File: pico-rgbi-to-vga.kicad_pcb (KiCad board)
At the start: 2 copper layers, 68.8 x 57 mm, 25 parts, among them J1 SDS-80J, J2 DB15_Female_HighDensity, J3 USB-B1HSB6, SW1 SW_Push, U1 Pico

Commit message: Fix label
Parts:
- RN1: value 20kΩ -> 15kΩ
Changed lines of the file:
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@@
     (descr "7-pin Resistor SIP pack")
     (tags "R")
+    (property "Mouser" "652-4607X-1LF-22K")
     (property "Sheetfile" "pico-rgbi-to-vga.kicad_sch")
     (property "Sheetname" "")
@@
       (effects (font (size 1 1) (thickness 0.15)))
     )
-    (fp_text value "20kΩ" (at 19.2 0.7 90) (layer "F.SilkS")
+    (fp_text value "15kΩ" (at 19.2 0.7 90) (layer "F.SilkS")
       (effects (font (size 1 1) (thickness 0.15)))
     )

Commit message: Use 8SIP for Vdiv pulldown, 7SIP is not available
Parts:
- RN1: footprint Resistor_THT:R_Array_SIP7 -> Resistor_THT:R_Array_SIP8
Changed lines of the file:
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@@
   (net 54 "+3V3")
   (net 55 "/SW_PALETTE_CHANGE")
+  (net 56 "unconnected-(RN1-Pad8)")
   (footprint "Resistor_SMD:R_0805_2012Metric_Pad1.20x1.40mm_HandSolder" (layer "F.Cu")
     (at 163.068 111.76)
@@
           ) (width 0) (fill yes))
       ))
+  )
+  (footprint "Resistor_THT:R_Array_SIP8" (layer "F.Cu")
+    (at 120.904 74.676 -90)
+    (descr "8-pin Resistor SIP pack")
+    (tags "R")
+    (property "Sheetfile" "pico-rgbi-to-vga.kicad_sch")
+    (property "Sheetname" "")
+    (attr through_hole)
+    (fp_text reference "RN1" (at -0.508 -2.4 90) (layer "F.SilkS")
+      (effects (font (size 1 1) (thickness 0.15)))
+    )
+    (fp_text value "15kΩ" (at 20.447 0.508 180) (layer "F.SilkS")
+      (effects (font (size 1 1) (thickness 0.15)))
+    )
+    (fp_text user "${REFERENCE}" (at 8.89 0 90) (layer "F.Fab")
+      (effects (font (size 1 1) (thickness 0.15)))
+    )
+    (fp_line (start -1.44 -1.4) (end -1.44 1.4) (layer "F.SilkS") (width 0.12))
+    (fp_line (start 19.22 -1.4) (end -1.44 -1.4) (layer "F.SilkS") (width 0.12))
+    (fp_line (start 1.27 -1.4) (end 1.27 1.4) (layer "F.SilkS") (width 0.12))
+    (fp_line (start -1.44 1.4) (end 19.22 1.4) (layer "F.SilkS") (width 0.12))
+    (fp_line (start 19.22 1.4) (end 19.22 -1.4) (layer "F.SilkS") (width 0.12))
+    (fp_line (start 19.5 1.65) (end 19.5 -1.65) (layer "F.CrtYd") (width 0.05))
+    (fp_line (start -1.7 1.65) (end 19.5 1.65) (layer "F.CrtYd") (width 0.05))
+    (fp_line (start 19.5 -1.65) (end -1.7 -1.65) (layer "F.CrtYd") (width 0.05))
+    (fp_line (start -1.7 -1.65) (end -1.7 1.65) (layer "F.CrtYd") (width 0.05))
+    (fp_line (start 19.07 -1.25) (end -1.29 -1.25) (layer "F.Fab") (width 0.1))
+    (fp_line (start 19.07 1.25) (end 19.07 -1.25) (layer "F.Fab") (width 0.1))
+    (fp_line (start 1.27 -1.25) (end 1.27 1.25) (layer "F.Fab") (width 0.1))
+    (fp_line (start -1.29 -1.25) (end -1.29 1.25) (layer "F.Fab") (width 0.1))
+    (fp_line (start -1.29 1.25) (end 19.07 1.25) (layer "F.Fab") (width 0.1))
+    (pad "1" thru_hole rect (at 0 0 270) (size 1.6 1.6) (drill 0.8) (layers *.Cu *.Mask)
+      (net 2 "GND") (pinfunction "common") (pintype "passive"))
+    (pad "2" thru_hole oval (at 2.54 0 270) (size 1.6 1.6) (drill 0.8) (layers *.Cu *.Mask)
+      (net 3 "/INTENS_IN") (pinfunction "R1") (pintype "passive"))
+    (pad "3" thru_hole oval (at 5.08 0 270) (size 1.6 1.6) (drill 0.8) (layers *.Cu *.Mask)
+      (net 5 "/VSYNC_IN") (pinfunction "R2") (pintype "passive"))
+    (pad "4" thru_hole oval (at 7.62 0 270) (size 1.6 1.6) (drill 0.8) (layers *.Cu *.Mask)
+      (net 4 "/HSYNC_IN") (pinfunction "R3") (pintype "passive"))
+    (pad "5" thru_hole oval (at 10.16 0 270) (size 1.6 1.6) (drill 0.8) (layers *.Cu *.Mask)
+      (net 8 "/BLUE_IN") (pinfunction "R4") (pintype "passive"))
+    (pad "6" thru_hole oval (at 12.7 0 270) (size 1.6 1.6) (drill 0.8) (layers *.Cu *.Mask)
+      (net 7 "/GREEN_IN") (pinfunction "R5") (pintype "passive"))
+    (pad "7" thru_hole oval (at 15.24 0 270) (size 1.6 1.6) (drill 0.8) (layers *.Cu *.Mask)
+      (net 6 "/RED_IN") (pinfunction "R6") (pintype "passive"))
+    (pad "8" thru_hole oval (at 17.78 0 270) (size 1.6 1.6) (drill 0.8) (layers *.Cu *.Mask)
+      (net 56 "unconnected-(RN1-Pad8)") (pinfunction "R7") (pintype "passive+no_connect"))
+    (model "${KICAD6_3DMODEL_DIR}/Resistor_THT.3dshapes/R_Array_SIP8.wrl"
+      (offset (xyz 0 0 0))
+      (scale (xyz 1 1 1))
+      (rotate (xyz 0 0 0))
+    )
   )
   (footprint "Resistor_SMD:R_0805_2012Metric_Pad1.20x1.40mm_HandSolder" (layer "F.Cu")
@@
       (offset (xyz 0 0 0))
       (scale (xyz 1 1 1))
-      (rotate (xyz 0 0 0))
-    )
-  )
-  (footprint "Resistor_THT:R_Array_SIP7" (layer "F.Cu")
-    (at 120.904 74.676 -90)
-    (descr "7-pin Resistor SIP pack")
-    (tags "R")
-    (property "Mouser" "652-4607X-1LF-22K")
-    (property "Sheetfile" "pico-rgbi-to-vga.kicad_sch")
-    (property "Sheetname" "")
-    (attr through_hole)
-    (fp_text reference "RN1" (at 18.7 -0.6 90) (layer "F.SilkS")
-      (effects (font (size 1 1) (thickness 0.15)))
-    )
-    (fp_text value "15kΩ" (at 19.2 0.7 90) (layer "F.SilkS")
-      (effects (font (size 1 1) (thickness 0.15)))
-    )
-    (fp_text user "${REFERENCE}" (at 7.62 0 90) (layer "F.Fab")
-      (effects (font (size 1 1) (thickness 0.15)))
-    )
-    (fp_line (start 16.68 1.4) (end 16.68 -1.4) (layer "F.SilkS") (width 0.12))
-    (fp_line (start -1.44 1.4) (end 16.68 1.4) (layer "F.SilkS") (width 0.12))
-    (fp_line (start 16.68 -1.4) (end -1.44 -1.4) (layer "F.SilkS") (width 0.12))
-    (fp_line (start 1.27 -1.4) (end 1.27 1.4) (layer "F.SilkS") (width 0.12))
-    (fp_line (start -1.44 -1.4) (end -1.44 1.4) (layer "F.SilkS") (width 0.12))
-    (fp_line (start -1.7 1.65) (end 16.95 1.65) (layer "F.CrtYd") (width 0.05))
-    (fp_line (start -1.7 -1.65) (end -1.7 1.65) (layer "F.CrtYd") (width 0.05))
-    (fp_line (start 16.95 -1.65) (end -1.7 -1.65) (layer "F.CrtYd") (width 0.05))
-    (fp_line (start 16.95 1.65) (end 16.95 -1.65) (layer "F.CrtYd") (width 0.05))
-    (fp_line (start 16.53 1.25) (end 16.53 -1.25) (layer "F.Fab") (width 0.1))
-    (fp_line (start -1.29 -1.25) (end -1.29 1.25) (layer "F.Fab") (width 0.1))
-    (fp_line (start -1.29 1.25) (end 16.53 1.25) (layer "F.Fab") (width 0.1))
-    (fp_line (start 16.53 -1.25) (end -1.29 -1.25) (layer "F.Fab") (width 0.1))
-    (fp_line (start 1.27 -1.25) (end 1.27 1.25) (layer "F.Fab") (width 0.1))
-    (pad "1" thru_hole rect (at 0 0 270) (size 1.6 1.6) (drill 0.8) (layers *.Cu *.Mask)
-      (net 2 "GND") (pinfunction "common") (pintype "passive"))
-    (pad "2" thru_hole oval (at 2.54 0 270) (size 1.6 1.6) (drill 0.8) (layers *.Cu *.Mask)
-      (net 3 "/INTENS_IN") (pinfunction "R1") (pintype "passive"))
-    (pad "3" thru_hole oval (at 5.08 0 270) (size 1.6 1.6) (drill 0.8) (layers *.Cu *.Mask)
-      (net 5 "/VSYNC_IN") (pinfunction "R2") (pintype "passive"))
-    (pad "4" thru_hole oval (at 7.62 0 270) (size 1.6 1.6) (drill 0.8) (layers *.Cu *.Mask)
-      (net 4 "/HSYNC_IN") (pinfunction "R3") (pintype "passive"))
-    (pad "5" thru_hole oval (at 10.16 0 270) (size 1.6 1.6) (drill 0.8) (layers *.Cu *.Mask)
-      (net 8 "/BLUE_IN") (pinfunction "R4") (pintype "passive"))
-    (pad "6" thru_hole oval (at 12.7 0 270) (size 1.6 1.6) (drill 0.8) (layers *.Cu *.Mask)
-      (net 7 "/GREEN_IN") (pinfunction "R5") (pintype "passive"))
-    (pad "7" thru_hole oval (at 15.24 0 270) (size 1.6 1.6) (drill 0.8) (layers *.Cu *.Mask)
-      (net 6 "/RED_IN") (pinfunction "R6") (pintype "passive"))
-    (model "${KICAD6_3DMODEL_DIR}/Resistor_THT.3dshapes/R_Array_SIP7.wrl"
-      (offset (xyz 0 0 0))
-      (scale (xyz 1 1 1))

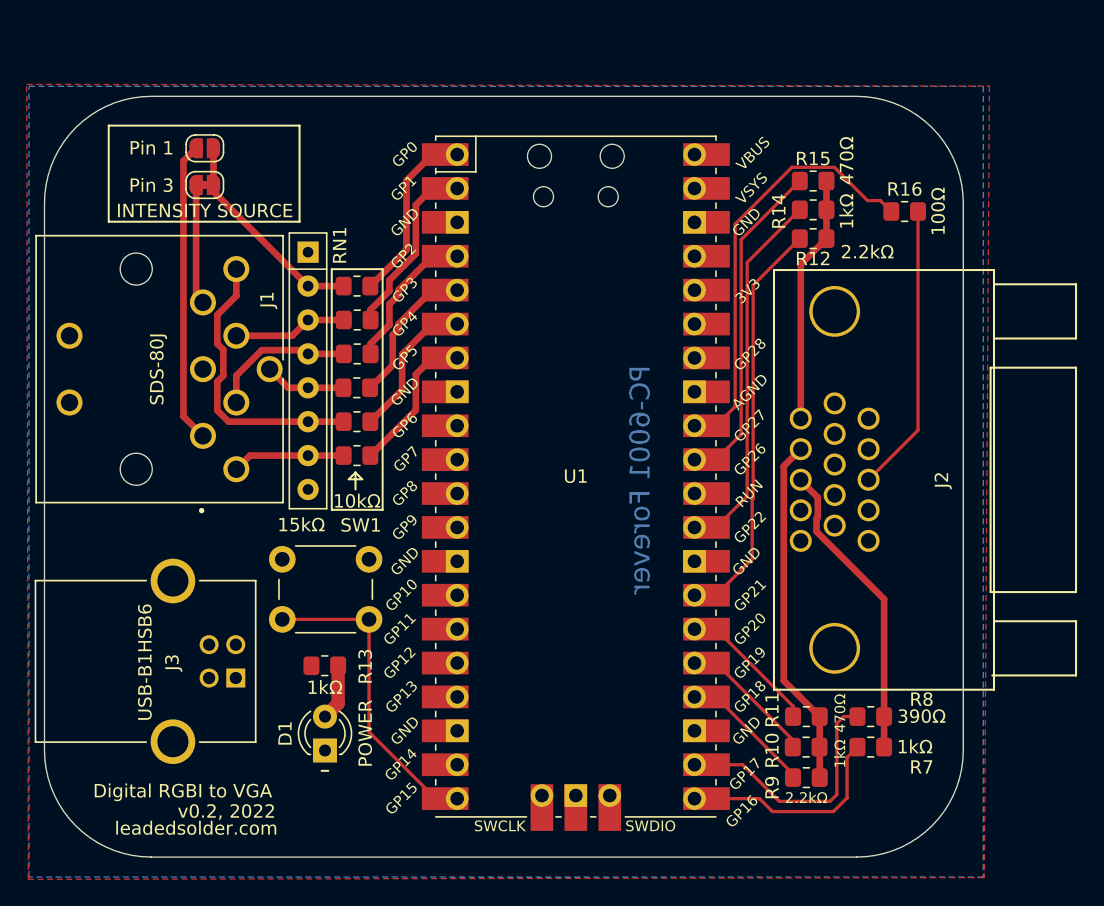
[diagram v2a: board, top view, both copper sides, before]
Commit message: Fix VGA output pins to use GPIOs that exist
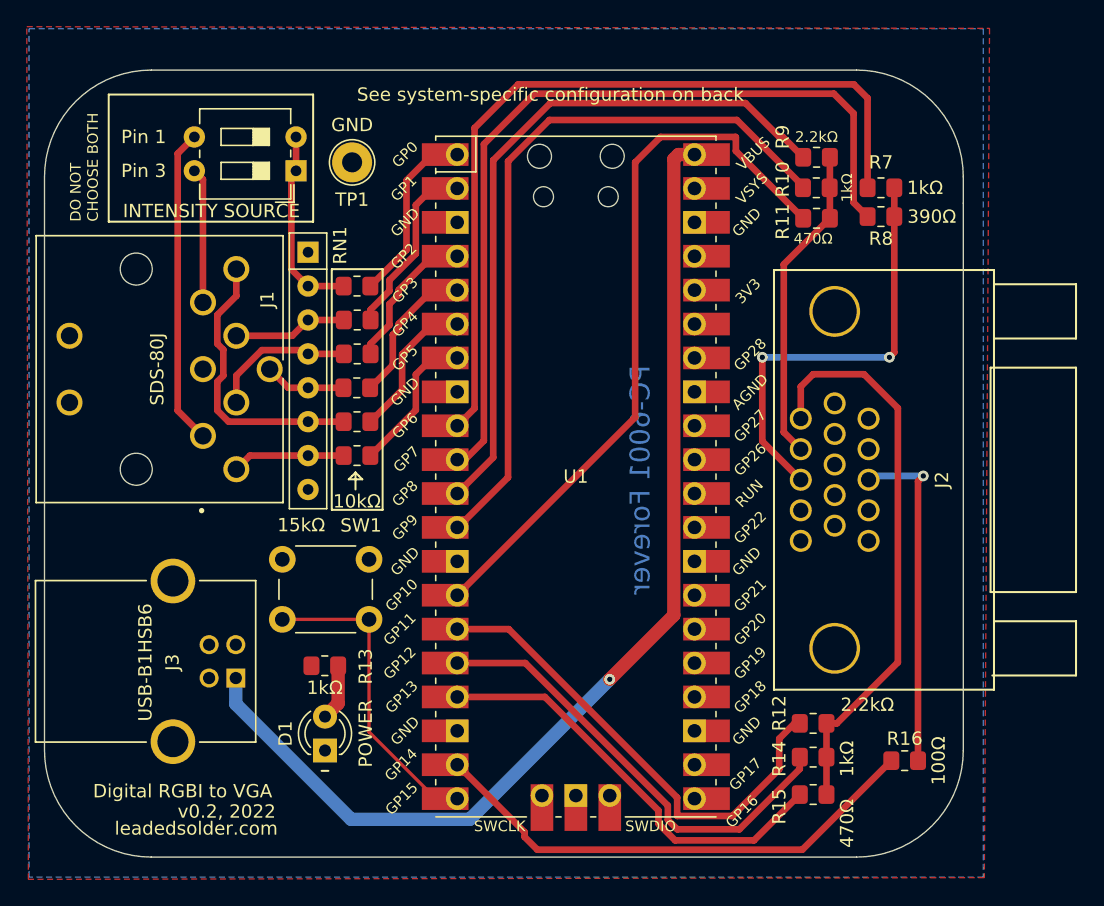
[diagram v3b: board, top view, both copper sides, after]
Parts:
- removed JP1: Jumper_2_Open, Jumper:SolderJumper-2_P1.3mm_Open_RoundedPad1.0x1.5mm
- removed JP2: Jumper_2_Bridged, Jumper:SolderJumper-2_P1.3mm_Bridged_RoundedPad1.0x1.5mm
- added SW2: Intensity Select, Button_Switch_THT:SW_DIP_SPSTx02_Slide_6.7x6.64mm_W7.62mm_P2.54mm_LowProfile, F.Cu at (120.0, 68.6)
- added TP1: GND, TestPoint:TestPoint_Loop_D2.54mm_Drill1.5mm_Beaded, F.Cu at (124.2, 67.9)
- moved R9 46.5 mm to (159.0, 67.6)
- moved R15 46.0 mm to (158.8, 115.3)
- moved R10 41.9 mm to (159.0, 69.8)
- moved R7 41.9 mm to (163.8, 69.8)
- moved R16 41.1 mm to (165.6, 112.8)
- moved R14 41.0 mm to (158.8, 112.5)
- moved R8 37.5 mm to (163.8, 72.0)
- moved R11 37.3 mm to (159.0, 72.1)
- moved R12 36.3 mm to (158.8, 110.0)
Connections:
- J1 pad 1: Net-(J1-Pad1) -> /DIN_VIDEO_PIN_1
- J1 pad 3: Net-(J1-Pad3) -> /DIN_VIDEO_PIN_3
- U1 pad 10: unconnected-(U1-Pad10) -> /PicoVGA_Blue1
- U1 pad 11: unconnected-(U1-Pad11) -> /PicoVGA_Green0
- U1 pad 12: unconnected-(U1-Pad12) -> /PicoVGA_Green1
- U1 pad 14: unconnected-(U1-Pad14) -> /PicoVGA_Green2
- U1 pad 15: unconnected-(U1-Pad15) -> /PicoVGA_Red0
- U1 pad 16: unconnected-(U1-Pad16) -> /PicoVGA_Red1
- U1 pad 17: unconnected-(U1-Pad17) -> /PicoVGA_Red2
- U1 pad 19: unconnected-(U1-Pad19) -> /PicoVGA_CSync
- U1 pad 21: /PicoVGA_Blue0 -> unconnected-(U1-Pad21)
- U1 pad 22: /PicoVGA_Blue1 -> unconnected-(U1-Pad22)
- U1 pad 24: /PicoVGA_Green0 -> unconnected-(U1-Pad24)
- U1 pad 25: /PicoVGA_Green1 -> unconnected-(U1-Pad25)
- U1 pad 26: /PicoVGA_Green2 -> unconnected-(U1-Pad26)
- U1 pad 27: /PicoVGA_Red0 -> unconnected-(U1-Pad27)
- U1 pad 29: /PicoVGA_Red1 -> unconnected-(U1-Pad29)
- U1 pad 31: /PicoVGA_Red2 -> unconnected-(U1-Pad31)
- U1 pad 32: /PicoVGA_CSync -> unconnected-(U1-Pad32)
- U1 pad 9: unconnected-(U1-Pad9) -> /PicoVGA_Blue0
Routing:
- net +5V: track 0.00 -> 80.5 mm, vias 0 -> 1
- net /PicoVGA_Blue0: track 16.4 -> 60.8 mm
- net /PicoVGA_Green1: track 10.3 -> 54.6 mm
- net /PicoVGA_Green2: track 10.6 -> 54.5 mm
- net /PicoVGA_Blue1: track 19.1 -> 62.9 mm
- net /PicoVGA_Green0: track 10.0 -> 52.8 mm
- net /RED_OUT: track 18.6 -> 42.7 mm
- net /DIN_VIDEO_PIN_1: track 0.00 -> 23.7 mm
- net Net-(J1-Pad1): track 22.5 -> 0.00 mm
- net /DIN_VIDEO_PIN_3: track 0.00 -> 10.8 mm
- net /BLUE_OUT: track 22.7 -> 32.7 mm, vias 0 -> 2
- net Net-(J1-Pad3): track 9.01 -> 0.00 mm
- net /PicoVGA_Red2: track 25.1 -> 32.1 mm
- net /PicoVGA_Red1: track 28.0 -> 34.2 mm
- net /PicoVGA_CSync: track 32.1 -> 38.1 mm
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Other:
- board size 68.8 x 57 mm -> 68.8 x 59 mm
- board text added: "DO NOT CHOOSE BOTH"
- board text added: "PC-8801mkII: DO NOT use intensity (+12V danger!)"
- board text added: "See system-specific configuration on back"

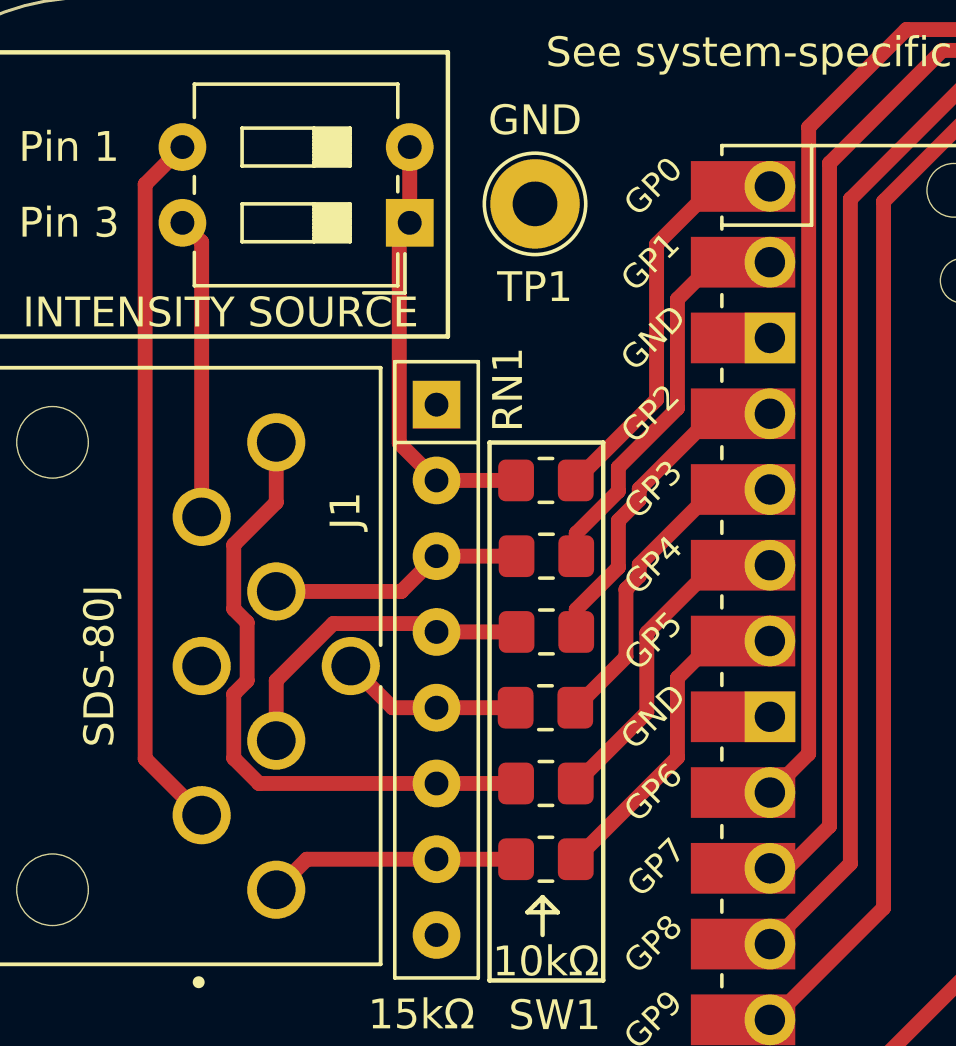
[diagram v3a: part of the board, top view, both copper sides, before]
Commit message: KiCad7; reorder pins so HV won't get captured
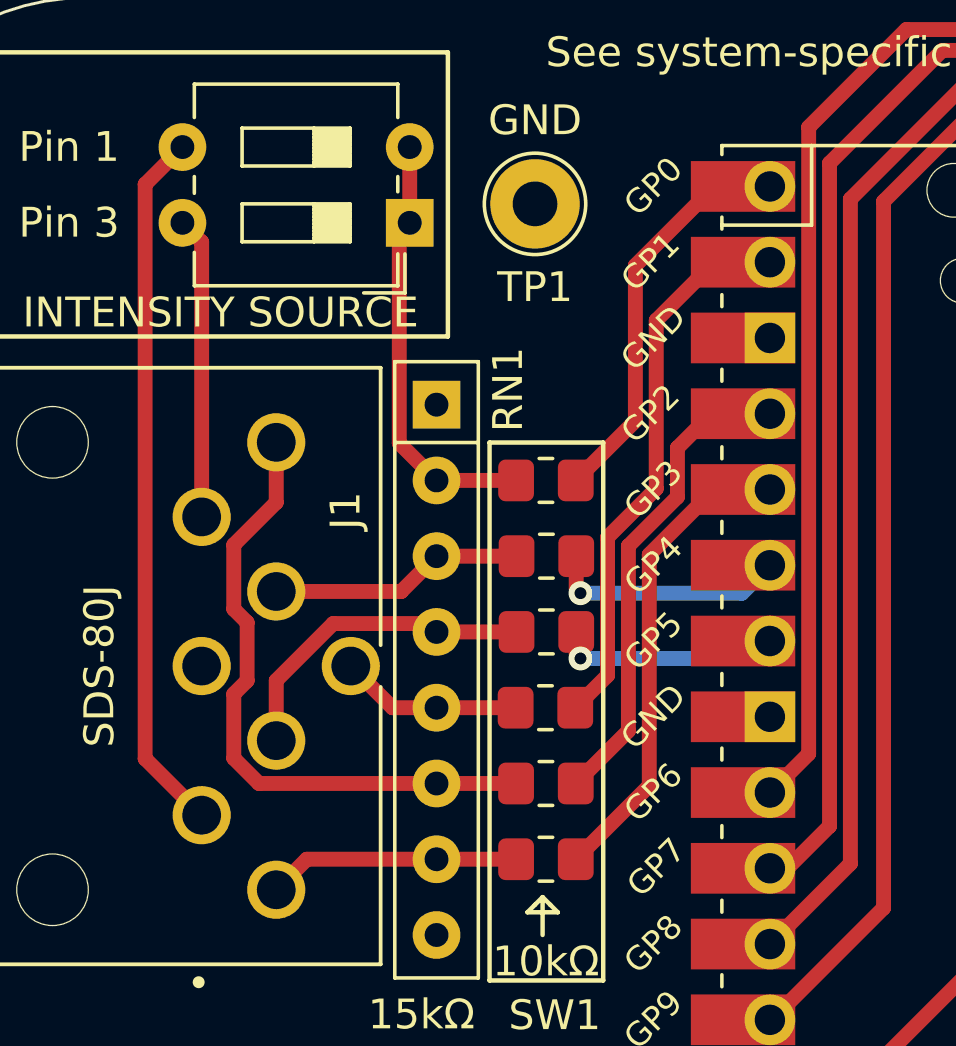
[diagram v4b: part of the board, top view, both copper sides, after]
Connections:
- U1 pad 2: /VSYNC_3v3 -> /BLUE_3v3
- U1 pad 4: /HSYNC_3v3 -> /GREEN_3v3
- U1 pad 5: /BLUE_3v3 -> /RED_3v3
- U1 pad 6: /GREEN_3v3 -> /VSYNC_3v3
- U1 pad 7: /RED_3v3 -> /HSYNC_3v3
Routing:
- net /BLUE_3v3: track 11.1 -> 18.7 mm
- net /VSYNC_3v3: track 13.6 -> 8.04 mm, vias 0 -> 1
- net /GREEN_3v3: track 11.1 -> 16.2 mm
- net /RED_3v3: track 11.1 -> 16.2 mm
- net /HSYNC_3v3: track 11.1 -> 7.54 mm, vias 0 -> 1
- net /DIN_VIDEO_PIN_3: track 10.8 -> 10.1 mm
